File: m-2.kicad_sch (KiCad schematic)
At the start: 20 parts, among them J503 Bus_M.2_1-2199230-6, M503 Mech_M2_2280_H2.5mm

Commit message: [#100765] Reset designators
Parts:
- renumbered C513 to C1, C514 to C2, C515 to C3, C516 to C4, C517 to C5, C518 to C6, D505 to D1, H503 to H9, J503 to J1, M503 to M1, R70 to R1, R507 to R2, R508 to R3, R509 to R4, R512 to R5, R30 to R6, TP509 to TP1, TP510 to TP2, TP511 to TP3, TP512 to TP4

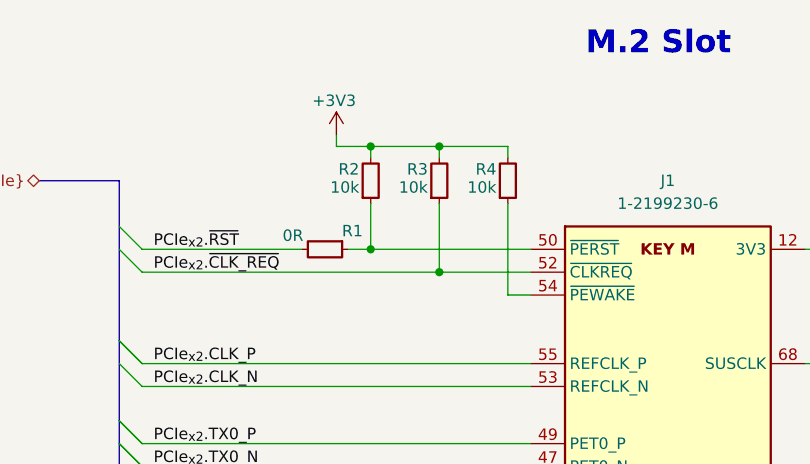
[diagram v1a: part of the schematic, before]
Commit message: [#100765] Prettify schematic
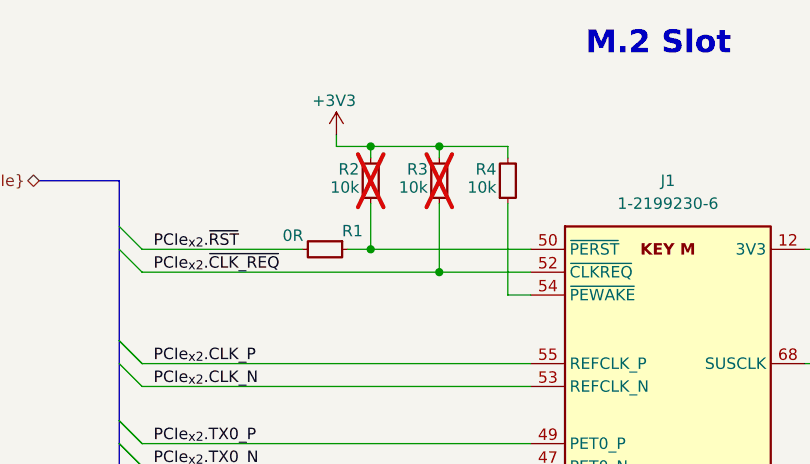
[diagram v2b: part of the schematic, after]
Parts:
- R2, R3: now not fitted
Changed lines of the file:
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@@
 		(on_board yes)
 		(in_pos_files yes)
-		(dnp no)
+		(dnp yes)
 		(property "Reference" "R3"
 			(at 181.61 109.22 90)
@@
 		(on_board yes)
 		(in_pos_files yes)
-		(dnp no)
+		(dnp yes)
 		(property "Reference" "R2"
 			(at 173.99 109.22 90)

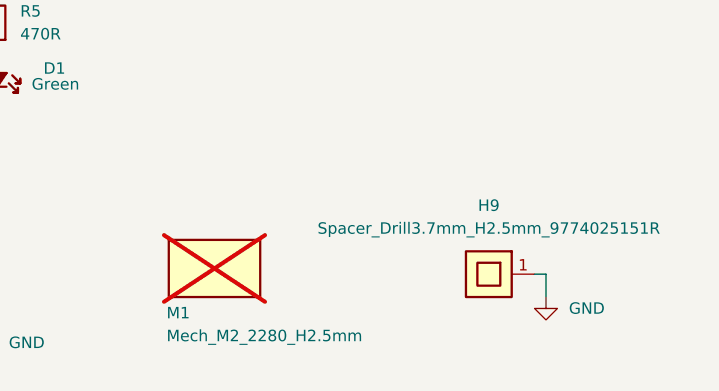
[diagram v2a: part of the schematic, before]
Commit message: [#100765] Fix legacy DNP & Remove obsolete spacer drills
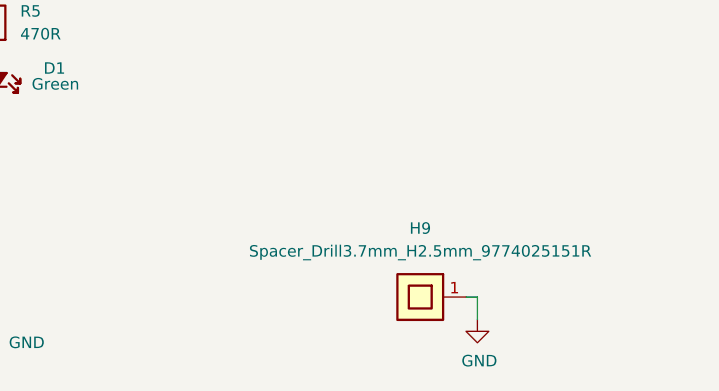
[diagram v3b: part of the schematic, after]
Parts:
- removed M1: Mech_M2_2280_H2.5mm, antmicro-footprints:Mech_M2_2280_H2.5mm, symbol antmicroModules:Mech_M2_2280_H2.5mm
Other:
- moved on the sheet: H9
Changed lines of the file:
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@@
 	(wire
 		(pts
-			(xy 287.02 190.5) (xy 287.02 193.04)
+			(xy 279.4 193.04) (xy 279.4 195.58)
 		)
 		(stroke
@@
 	(wire
 		(pts
-			(xy 285.75 190.5) (xy 287.02 190.5)
+			(xy 278.13 193.04) (xy 279.4 193.04)
 		)
 		(stroke
@@
 	(symbol
 		(lib_id "antmicropower:GND")
-		(at 287.02 193.04 0)
+		(at 279.4 195.58 0)
 		(mirror y)
 		(unit 1)
@@
 		(in_pos_files yes)
 		(dnp no)
-		(fields_autoplaced yes)
 		(property "Reference" "#PWR08"
-			(at 278.13 195.58 0)
+			(at 270.51 198.12 0)
 			(hide yes)
 			(show_name no)
@@
 		)
 		(property "Value" "GND"
-			(at 289.56 194.31 0)
+			(at 277.622 200.152 0)
 			(show_name no)
 			(do_not_autoplace no)
@@
 		)
 		(property "Footprint" ""
-			(at 278.13 200.66 0)
+			(at 270.51 203.2 0)
 			(hide yes)
 			(show_name no)
@@
 		)
 		(property "Datasheet" ""
-			(at 278.13 205.74 0)
+			(at 270.51 208.28 0)
 			(hide yes)
 			(show_name no)
@@
 		)
 		(property "Description" ""
-			(at 278.13 208.28 0)
+			(at 270.51 210.82 0)
 			(hide yes)
 			(show_name no)
@@
 		)
 		(property "Author" "Antmicro"
-			(at 278.13 200.66 0)
+			(at 270.51 203.2 0)
 			(hide yes)
 			(show_name no)
@@
 		)
 		(property "License" "Apache-2.0"
-			(at 278.13 203.2 0)
+			(at 270.51 205.74 0)
 			(hide yes)
 			(show_name no)
@@
 	(symbol
 		(lib_id "antmicroMechanicalParts:Spacer_Drill3.7mm_H2.5mm_9774025151R")
-		(at 285.75 190.5 180)
+		(at 278.13 193.04 180)
 		(unit 1)
 		(body_style 1)
@@
 		(fields_autoplaced yes)
 		(property "Reference" "H9"
-			(at 280.67 182.88 0)
+			(at 273.05 185.42 0)
 			(show_name no)
 			(do_not_autoplace no)
@@
 		)
 		(property "Value" "Spacer_Drill3.7mm_H2.5mm_9774025151R"
-			(at 280.67 185.42 0)
+			(at 273.05 187.96 0)
 			(show_name no)
 			(do_not_autoplace no)
@@
 		)
 		(property "Footprint" "antmicro-footprints:Spacer_Drill3.7mm_H2.5mm_9774025151R"
-			(at 262.89 182.88 0)
+			(at 255.27 185.42 0)
 			(hide yes)
 			(show_name no)
@@
 		)
 		(property "Datasheet" "https://www.we-online.com/components/products/datasheet/9774025151R.pdf"
-			(at 262.89 180.34 0)
+			(at 255.27 182.88 0)
 			(hide yes)
 			(show_name no)
@@
 		)
 		(property "Description" "Spacer, SMT, Non Stop, Steel, Swage Round, 5.1 mm x 2.5 mm, M2.5 Thread, WA-SMSI Series"
-			(at 262.89 167.64 0)
+			(at 255.27 170.18 0)
 			(hide yes)
 			(show_name no)
@@
 		)
 		(property "Manufacturer" "Würth Elektronik"
-			(at 262.89 177.8 0)
+			(at 255.27 180.34 0)
 			(hide yes)
 			(show_name no)
@@
 		)
 		(property "MPN" "9774025151R"
-			(at 262.89 175.26 0)
+			(at 255.27 177.8 0)
 			(hide yes)
 			(show_name no)
@@
 		)
 		(property "Author" "Antmicro"
-			(at 262.89 172.72 0)
+			(at 255.27 175.26 0)
 			(hide yes)
 			(show_name no)
@@
 		)
 		(property "License" "Apache-2.0"
-			(at 262.89 170.18 0)
+			(at 255.27 172.72 0)
 			(hide yes)
 			(show_name no)
@@
 					(unit 1)
 				)
-			)
-		)
-	)
-	(symbol
-		(lib_id "antmicroModules:Mech_M2_2280_H2.5mm")
-		(at 255.27 193.04 180)
-		(unit 1)
-		(body_style 1)
-		(exclude_from_sim no)
-		(in_bom no)
-		(on_board yes)
-		(in_pos_files yes)
-		(dnp yes)
-		(property "Reference" "M1"
-			(at 244.856 194.8179 0)
-			(show_name no)
-			(do_not_autoplace no)
-			(effects
-				(font
-					(size 1.27 1.27)
-				)
-				(justify right)
-			)
-		)
-		(property "Value" "Mech_M2_2280_H2.5mm"
-			(at 244.856 197.358 0)
-			(show_name no)
-			(do_not_autoplace no)
-			(effects
-				(font
-					(size 1.27 1.27)
-					(thickness 0.15)
-				)
-				(justify right)
-			)
-		)
-		(property "Footprint" "antmicro-footprints:Mech_M2_2280_H2.5mm"
-			(at 229.87 187.96 0)
-			(hide yes)
-			(show_name no)
-			(do_not_autoplace no)
-			(effects
-				(font
-					(size 1.27 1.27)
-					(thickness 0.15)
-				)
-				(justify left bottom)
-			)
-		)
-		(property "Datasheet" ""
-			(at 229.87 185.42 0)
-			(hide yes)
-			(show_name no)
-			(do_not_autoplace no)
-			(effects
-				(font
-					(size 1.27 1.27)
-					(thickness 0.15)
-				)
-				(justify left bottom)
-			)
-		)
-		(property "Description" "Mechanical model for M2 2280 2.5mm module"
-			(at 229.87 177.8 0)
-			(hide yes)
-			(show_name no)
-			(do_not_autoplace no)
-			(effects
-				(font
-					(size 1.27 1.27)
-				)
-				(justify left bottom)
-			)
-		)
-		(property "Manufacturer" ""
-			(at 255.27 193.04 0)
-			(hide yes)
-			(show_name no)
-			(do_not_autoplace no)
-			(effects
-				(font
-					(size 1.27 1.27)
-				)
-			)
-		)
-		(property "MPN" ""
-			(at 255.27 193.04 0)
-			(show_name no)
-			(do_not_autoplace no)
-			(effects
-				(font
-					(size 1.27 1.27)
-				)
-			)
-		)
-		(property "Author" "Antmicro"
-			(at 229.87 182.88 0)
-			(hide yes)
-			(show_name no)
-			(do_not_autoplace no)
-			(effects
-				(font
-					(size 1.27 1.27)
-					(thickness 0.15)
-				)
-				(justify left bottom)
-			)
-		)
-		(property "License" "Apache-2.0"
-			(at 229.87 180.34 0)
-			(hide yes)
-			(show_name no)
-			(do_not_autoplace no)
-			(effects
-				(font
-					(size 1.27 1.27)
-					(thickness 0.15)
-				)
-				(justify left bottom)
-			)
-		)
-		(instances
-			(project "antmicro-jetson-orin-baseboard-pcie-switch-expansion-hw"
-				(path "/9f8272ef-d62d-4578-9094-a2852fcd4bf4/31e02060-3da3-4672-957a-70d1fbeafe0b"
-					(reference "M2")
-					(unit 1)
-				)
-				(path "/9f8272ef-d62d-4578-9094-a2852fcd4bf4/b5c79c47-5cbe-4246-8e95-1b16ae33d230"
-					(reference "M1")
-					(unit 1)
-				)

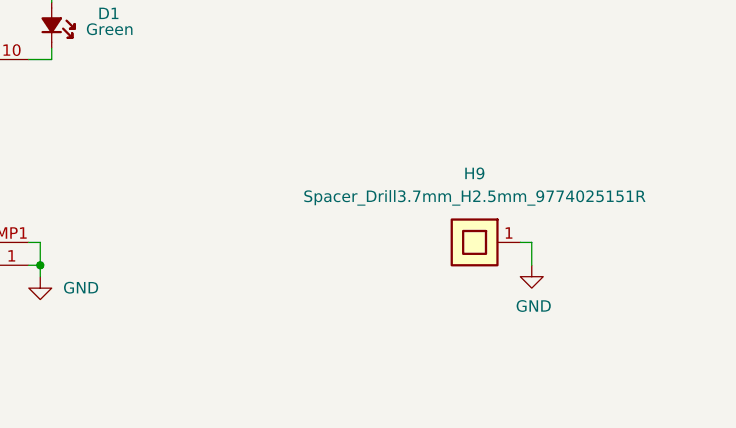
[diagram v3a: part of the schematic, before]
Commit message: [#101557] Add spacers from 2242 M.2 disks
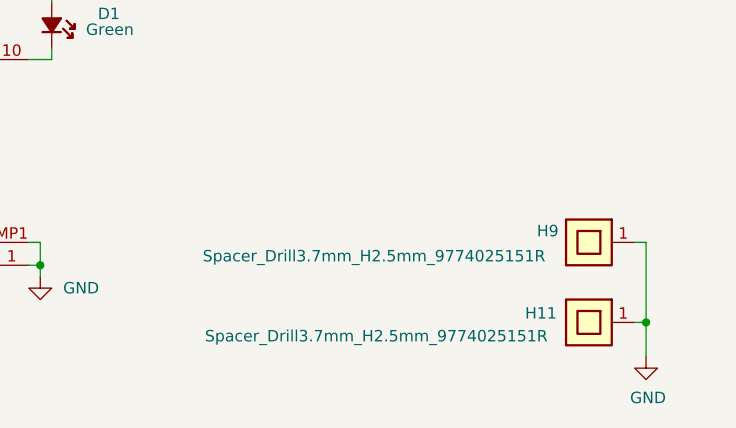
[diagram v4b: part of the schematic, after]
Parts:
- added H11: Spacer_Drill3.7mm_H2.5mm_9774025151R, antmicro-footprints:Spacer_Drill3.7mm_H2.5mm_9774025151R, symbol antmicroMechanicalParts:Spacer_Drill3.7mm_H2.5mm_9774025151R
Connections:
- net GND: now also H11.1
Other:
- moved on the sheet: H9
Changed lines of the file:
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@@
 	)
 	(junction
+		(at 292.1 201.93)
+		(diameter 0)
+		(color 0 0 0 0)
+	)
+	(junction
 		(at 182.88 120.65)
 		(diameter 0)
@@
 	(wire
 		(pts
-			(xy 279.4 193.04) (xy 279.4 195.58)
+			(xy 149.86 162.56) (xy 193.04 162.56)
 		)
 		(stroke
@@
 	(wire
 		(pts
-			(xy 149.86 162.56) (xy 193.04 162.56)
+			(xy 223.52 118.11) (xy 237.49 118.11)
 		)
 		(stroke
@@
 	(wire
 		(pts
-			(xy 223.52 118.11) (xy 237.49 118.11)
+			(xy 226.06 171.45) (xy 226.06 172.72)
 		)
 		(stroke
@@
 	(wire
 		(pts
-			(xy 226.06 171.45) (xy 226.06 172.72)
+			(xy 292.1 193.04) (xy 292.1 201.93)
 		)
 		(stroke
@@
 	(wire
 		(pts
+			(xy 290.83 201.93) (xy 292.1 201.93)
+		)
+		(stroke
+			(width 0)
+			(type default)
+		)
+	)
+	(wire
+		(pts
 			(xy 276.86 130.81) (xy 280.67 130.81)
 		)
@@
 		)
 	)
+	(wire
+		(pts
+			(xy 292.1 201.93) (xy 292.1 205.74)
+		)
+		(stroke
+			(width 0)
+			(type default)
+		)
+	)
 	(bus
 		(pts
@@
 	(wire
 		(pts
-			(xy 278.13 193.04) (xy 279.4 193.04)
+			(xy 290.83 193.04) (xy 292.1 193.04)
 		)
 		(stroke
@@
 	(symbol
 		(lib_id "antmicropower:GND")
-		(at 279.4 195.58 0)
+		(at 292.1 205.74 0)
 		(mirror y)
 		(unit 1)
@@
 		(dnp no)
 		(property "Reference" "#PWR08"
-			(at 270.51 198.12 0)
+			(at 283.21 208.28 0)
 			(hide yes)
 			(show_name no)
@@
 		)
 		(property "Value" "GND"
-			(at 277.622 200.152 0)
+			(at 290.322 210.312 0)
 			(show_name no)
 			(do_not_autoplace no)
@@
 		)
 		(property "Footprint" ""
-			(at 270.51 203.2 0)
+			(at 283.21 213.36 0)
 			(hide yes)
 			(show_name no)
@@
 		)
 		(property "Datasheet" ""
-			(at 270.51 208.28 0)
+			(at 283.21 218.44 0)
 			(hide yes)
 			(show_name no)
@@
 		)
 		(property "Description" ""
-			(at 270.51 210.82 0)
+			(at 283.21 220.98 0)
 			(hide yes)
 			(show_name no)
@@
 		)
 		(property "Author" "Antmicro"
-			(at 270.51 203.2 0)
+			(at 283.21 213.36 0)
 			(hide yes)
 			(show_name no)
@@
 		)
 		(property "License" "Apache-2.0"
-			(at 270.51 205.74 0)
+			(at 283.21 215.9 0)
 			(hide yes)
 			(show_name no)
@@
 	(symbol
 		(lib_id "antmicroMechanicalParts:Spacer_Drill3.7mm_H2.5mm_9774025151R")
-		(at 278.13 193.04 180)
+		(at 290.83 193.04 180)
 		(unit 1)
 		(body_style 1)
@@
 		(in_pos_files yes)
 		(dnp no)
-		(fields_autoplaced yes)
 		(property "Reference" "H9"
-			(at 273.05 185.42 0)
+			(at 281.178 191.77 0)
 			(show_name no)
 			(do_not_autoplace no)
@@
 		)
 		(property "Value" "Spacer_Drill3.7mm_H2.5mm_9774025151R"
-			(at 273.05 187.96 0)
+			(at 261.874 194.564 0)
 			(show_name no)
 			(do_not_autoplace no)
@@
 		)
 		(property "Footprint" "antmicro-footprints:Spacer_Drill3.7mm_H2.5mm_9774025151R"
-			(at 255.27 185.42 0)
+			(at 267.97 185.42 0)
 			(hide yes)
 			(show_name no)
@@
 		)
 		(property "Datasheet" "https://www.we-online.com/components/products/datasheet/9774025151R.pdf"
-			(at 255.27 182.88 0)
+			(at 267.97 182.88 0)
 			(hide yes)
 			(show_name no)
@@
 		)
 		(property "Description" "Spacer, SMT, Non Stop, Steel, Swage Round, 5.1 mm x 2.5 mm, M2.5 Thread, WA-SMSI Series"
-			(at 255.27 170.18 0)
+			(at 267.97 170.18 0)
 			(hide yes)
 			(show_name no)
@@
 		)
 		(property "Manufacturer" "Würth Elektronik"
-			(at 255.27 180.34 0)
+			(at 267.97 180.34 0)
 			(hide yes)
 			(show_name no)
@@
 		)
 		(property "MPN" "9774025151R"
-			(at 255.27 177.8 0)
+			(at 267.97 177.8 0)
 			(hide yes)
 			(show_name no)
@@
 		)
 		(property "Author" "Antmicro"
-			(at 255.27 175.26 0)
+			(at 267.97 175.26 0)
 			(hide yes)
 			(show_name no)
@@
 		)
 		(property "License" "Apache-2.0"
-			(at 255.27 172.72 0)
+			(at 267.97 172.72 0)
 			(hide yes)
 			(show_name no)
@@
 					(unit 1)
 				)
+			)
+		)
+	)
+	(symbol
+		(lib_id "antmicroMechanicalParts:Spacer_Drill3.7mm_H2.5mm_9774025151R")
+		(at 290.83 201.93 180)
+		(unit 1)
+		(body_style 1)
+		(exclude_from_sim no)
+		(in_bom yes)
+		(on_board yes)
+		(in_pos_files yes)
+		(dnp no)
+		(property "Reference" "H11"
+			(at 280.416 200.914 0)
+			(show_name no)
+			(do_not_autoplace no)
+			(effects
+				(font
+					(size 1.27 1.27)
+					(thickness 0.15)
+				)
+			)
+		)
+		(property "Value" "Spacer_Drill3.7mm_H2.5mm_9774025151R"
+			(at 262.128 203.454 0)
+			(show_name no)
+			(do_not_autoplace no)
+			(effects
+				(font
+					(size 1.27 1.27)
+					(thickness 0.15)
+				)
+			)
+		)
+		(property "Footprint" "antmicro-footprints:Spacer_Drill3.7mm_H2.5mm_9774025151R"
+			(at 267.97 194.31 0)
+			(hide yes)
+			(show_name no)
+			(do_not_autoplace no)
+			(effects
+				(font
+					(size 1.27 1.27)
+					(thickness 0.15)
+				)
+				(justify left bottom)
+			)
+		)
+		(property "Datasheet" "https://www.we-online.com/components/products/datasheet/9774025151R.pdf"
+			(at 267.97 191.77 0)
+			(hide yes)
+			(show_name no)
+			(do_not_autoplace no)
+			(effects
+				(font
+					(size 1.27 1.27)
+					(thickness 0.15)
+				)
+				(justify left bottom)
+			)
+		)
+		(property "Description" "Spacer, SMT, Non Stop, Steel, Swage Round, 5.1 mm x 2.5 mm, M2.5 Thread, WA-SMSI Series"
+			(at 267.97 179.07 0)
+			(hide yes)
+			(show_name no)
+			(do_not_autoplace no)
+			(effects
+				(font
+					(size 1.27 1.27)
+				)
+				(justify left bottom)
+			)
+		)
+		(property "Manufacturer" "Würth Elektronik"
+			(at 267.97 189.23 0)
+			(hide yes)
+			(show_name no)
+			(do_not_autoplace no)
+			(effects
+				(font
+					(size 1.27 1.27)
+					(thickness 0.15)
+				)
+				(justify left bottom)
+			)
+		)
+		(property "MPN" "9774025151R"
+			(at 267.97 186.69 0)
+			(hide yes)
+			(show_name no)
+			(do_not_autoplace no)
+			(effects
+				(font
+					(size 1.27 1.27)
+					(thickness 0.15)
+				)
+				(justify left bottom)
+			)
+		)
+		(property "Author" "Antmicro"
+			(at 267.97 184.15 0)
+			(hide yes)
+			(show_name no)
+			(do_not_autoplace no)
+			(effects
+				(font
+					(size 1.27 1.27)
+					(thickness 0.15)
+				)
+				(justify left bottom)
+			)
+		)
+		(property "License" "Apache-2.0"
+			(at 267.97 181.61 0)
+			(hide yes)
+			(show_name no)
+			(do_not_autoplace no)
+			(effects
+				(font
+					(size 1.27 1.27)
+					(thickness 0.15)
+				)
+				(justify left bottom)
+			)
+		)
+		(pin "1"
+		)
+		(instances
+			(project "antmicro-jetson-orin-baseboard-pcie-switch-expansion-hw"
+				(path "/9f8272ef-d62d-4578-9094-a2852fcd4bf4/31e02060-3da3-4672-957a-70d1fbeafe0b"
+					(reference "H12")
+					(unit 1)
+				)
+				(path "/9f8272ef-d62d-4578-9094-a2852fcd4bf4/b5c79c47-5cbe-4246-8e95-1b16ae33d230"
+					(reference "H11")
+					(unit 1)
+				)

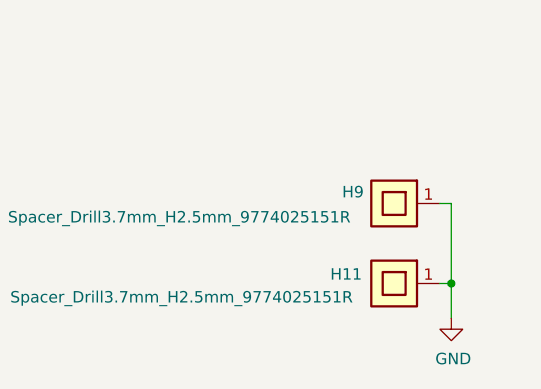
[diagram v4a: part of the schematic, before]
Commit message: [#101859] Change 2242 M.2 drilled mounts to DNP
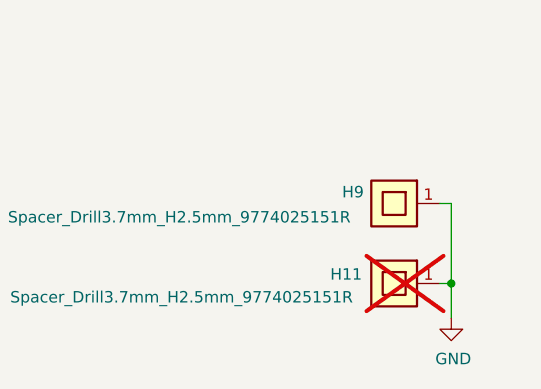
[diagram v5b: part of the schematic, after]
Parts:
- H11: now not fitted
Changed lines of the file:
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@@
 		(on_board yes)
 		(in_pos_files yes)
-		(dnp no)
+		(dnp yes)
 		(property "Reference" "H11"
 			(at 280.416 200.914 0)
